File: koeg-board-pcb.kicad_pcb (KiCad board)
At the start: 2 copper layers, 112.5 x 84.2 mm, 108 parts, among them J1 Conn_01x02, J2 SWD_Connector, J3 USB_C_Receptacle_USB2.0_14P, Q1 BSS138, SW1 Reset Button, SW10 SW_Push, SW11 SW_Push, SW12 SW_Push, SW13 SW_Push, SW14 SW_Push, SW15 SW_Push, SW16 SW_Push, SW17 SW_Push, SW18 SW_Push, SW19 SW_Push, SW2 SW_On_Off, SW20 SW_Push, SW21 SW_Push, SW22 SW_Push, SW23 SW_Push, SW3 SW_Push, SW4 SW_Push, SW5 SW_Push, SW6 SW_Push, SW7 SW_Push, SW8 SW_Push, SW9 SW_Push, U1 nRF52840, U2 USBLC6-2SC6, U3 AMS1117-5.0, Y1 JYJE 2TJ432000NYFBC

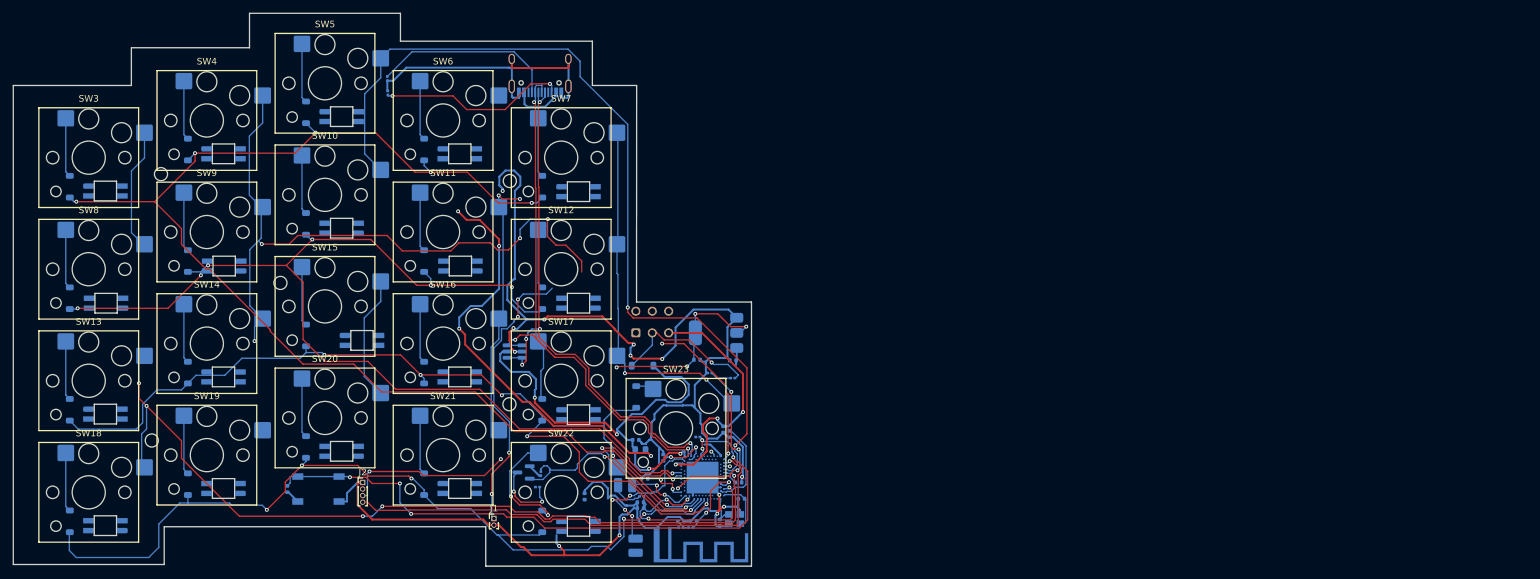
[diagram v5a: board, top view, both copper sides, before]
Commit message: routed left side
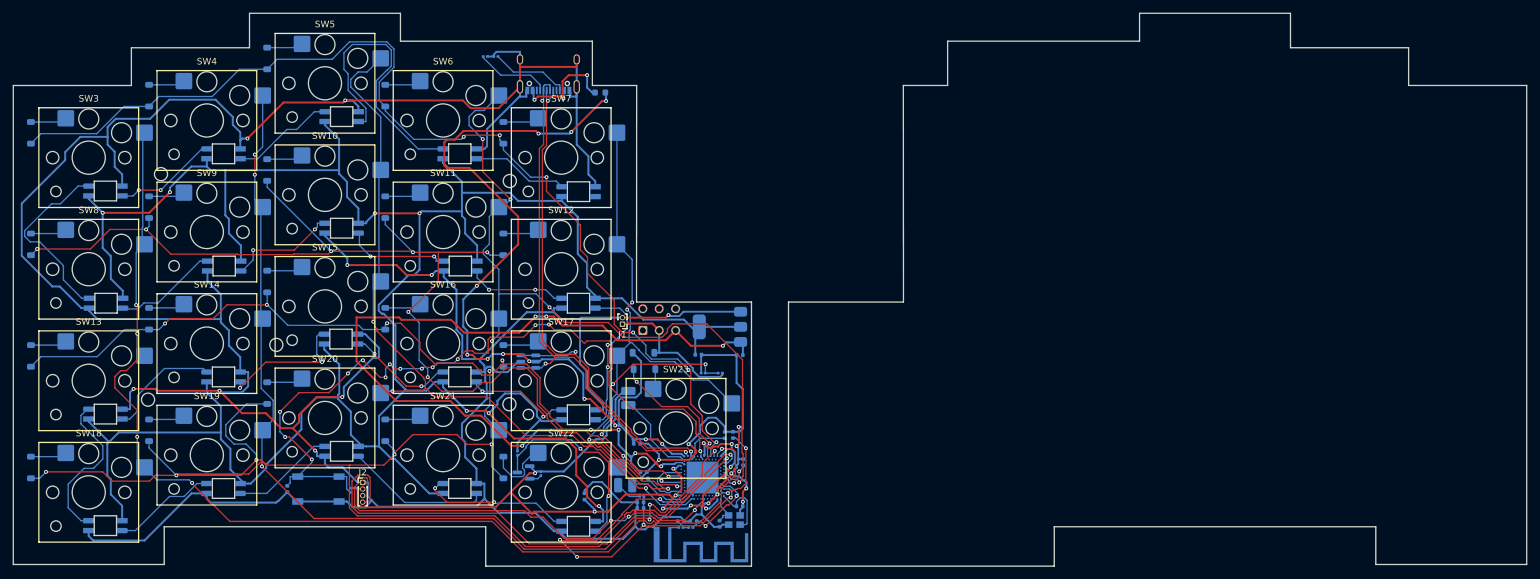
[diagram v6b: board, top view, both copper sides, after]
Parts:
- J3: footprint USB_Type_C:HRO-TYPE-C-31-M-12 -> Connector_USB:USB_C_Receptacle_XKB_U262-16XN-4BVC11
- moved F1 54.7 mm to (123.0, 55.8), turned to 180 degrees
- moved R1 53.5 mm to (85.1, 116.4), turned to -90 degrees
- moved J1 35.5 mm to (126.4, 91.1), turned to 180 degrees
- moved L3 22.5 mm to (127.3, 102.3), turned to 90 degrees
- moved R5 17.4 mm to (107.1, 50.3), turned to 180 degrees
- moved R4 15.3 mm to (105.5, 50.3), turned to 0 degrees
- moved C3 13.7 mm to (129.7, 113.6), turned to 0 degrees
- moved D2 10.1 mm to (36.3, 61.9)
- moved D12 10.1 mm to (36.3, 95.9)
- moved D13 10.1 mm to (54.3, 90.2)
- moved D17 10.1 mm to (36.3, 112.9)
- moved D18 10.1 mm to (54.3, 107.2)
- moved D3 10.1 mm to (54.3, 56.2)
- moved D7 10.1 mm to (36.3, 78.9)
- moved D8 10.1 mm to (54.3, 73.2)
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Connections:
- U1 pad A10: /left/ROW4 -> unconnected-(U1-AIN5/P0.29-PadA10)
- U1 pad A16: /left/ROW2 -> unconnected-(U1-P1.13-PadA16)
- U1 pad A8: /left/ROW0 -> /left/COL2
- U1 pad AD16: unconnected-(U1-P0.20-PadAD16) -> /left/ROW4
- U1 pad AD18: unconnected-(U1-P0.22-PadAD18) -> /left/ROW0
- U1 pad AD22: unconnected-(U1-TRACEDATA0/P1.00-PadAD22) -> /left/COL0
- U1 pad J1: unconnected-(U1-AIN2/P0.04-PadJ1) -> /left/ROW2
- U1 pad R24: /left/COL0 -> unconnected-(U1-P1.06-PadR24)
- U1 pad U24: /left/COL2 -> unconnected-(U1-P1.04-PadU24)
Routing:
- net LED_5V: track 29.8 -> 405.4 mm, vias 4 -> 7
- net GND: track 311.5 -> 652.2 mm, vias 13 -> 18
- net V_SYS: track 5.65 -> 127.8 mm, vias 0 -> 10
- net 3.2V-5V: track 42.2 -> 136.5 mm, vias 3 -> 8
- net /left/COL3: track 41.7 -> 127.5 mm, vias 3 -> 6
- net 5V: track 66.7 -> 129.9 mm, vias 4 -> 12
- net /left/ROW3: track 131.2 -> 188.4 mm, vias 5 -> 6
- net VBUS: track 73.0 -> 17.4 mm, vias 4 -> 3
- net VBAT: track 66.7 -> 22.0 mm, vias 5 -> 0
- net Net-(D39-DIN): track 0.00 -> 43.6 mm
- net /left/COL1: track 102.8 -> 144.1 mm, vias 5 -> 6
- net /left/COL2: track 151.0 -> 114.9 mm, vias 2 -> 3
- net /left/leds/LED_PIN: track 35.3 -> 1.89 mm, vias 2 -> 0
- net /left/ROW0: track 192.1 -> 160.3 mm
- net Net-(D37-DOUT): track 0.00 -> 28.5 mm
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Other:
- board size 112.5 x 84.2 mm -> 230.6 x 84.3 mm

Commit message: placed right side
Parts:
- added AE2: PCB_Antenna, pcb_ant:pcb_antenna, F.Cu at (167.2, 122.4)
- added C17: 4.7uF, Capacitor_SMD:C_0402_1005Metric, B.Cu at (156.7, 115.3)
- added C18: 100nF, Capacitor_SMD:C_0402_1005Metric, B.Cu at (227.4, 116.5)
- added C19: 4.7uF, Capacitor_SMD:C_0402_1005Metric, B.Cu at (156.7, 116.5)
- added C20: 100nF, Capacitor_SMD:C_0402_1005Metric, B.Cu at (174.6, 120.6)
- added C21: 100pF, Capacitor_SMD:C_0402_1005Metric, B.Cu at (172.5, 110.8)
- added C22: 820pF, Capacitor_SMD:C_0402_1005Metric, B.Cu at (156.7, 113.7)
- added C23: 1uF, Capacitor_SMD:C_0402_1005Metric, B.Cu at (174.8, 117.8)
- added C24: 47nF, Capacitor_SMD:C_0402_1005Metric, B.Cu at (174.8, 116.7)
- added C25: 4.7uF, Capacitor_SMD:C_0402_1005Metric, B.Cu at (156.7, 117.7)
- added C26: 4.7uF, Capacitor_SMD:C_0402_1005Metric, B.Cu at (174.6, 122.6)
- added C27: 12pF, Capacitor_SMD:C_0402_1005Metric, B.Cu at (177.3, 108.0)
- added C28: 12pF, Capacitor_SMD:C_0402_1005Metric, B.Cu at (172.7, 108.3)
- added C29: 1pF, Capacitor_SMD:C_0402_1005Metric, B.Cu at (171.2, 125.9)
- added C30: 1.2pF, Capacitor_SMD:C_0402_1005Metric, B.Cu at (171.2, 124.1)
- added C31: 1uF, Capacitor_SMD:C_0402_1005Metric, B.Cu at (156.7, 97.7)
- added C32: 1uF, Capacitor_SMD:C_0402_1005Metric, B.Cu at (156.8, 96.3)
- added D43: 1N5819, Diode_SMD:D_SOD-123, B.Cu at (173.0, 84.5)
- added D44: 1N5819, Diode_SMD:D_SOD-123, B.Cu at (247.0, 61.9)
- added D45: 1N5819, Diode_SMD:D_SOD-123, B.Cu at (229.0, 56.2)
- added D46: 1N5819, Diode_SMD:D_SOD-123, B.Cu at (211.0, 50.6)
- added D47: 1N5819, Diode_SMD:D_SOD-123, B.Cu at (193.0, 56.2)
- added D48: 1N5819, Diode_SMD:D_SOD-123, B.Cu at (175.0, 61.9)
- added D49: 1N5819, Diode_SMD:D_SOD-123, B.Cu at (247.0, 78.9)
- added D50: 1N5819, Diode_SMD:D_SOD-123, B.Cu at (229.0, 73.2)
- added D51: 1N5819, Diode_SMD:D_SOD-123, B.Cu at (211.0, 67.6)
- added D52: 1N5819, Diode_SMD:D_SOD-123, B.Cu at (193.0, 73.2)
- added D53: 1N5819, Diode_SMD:D_SOD-123, B.Cu at (175.0, 78.9)
- added D54: 1N5819, Diode_SMD:D_SOD-123, B.Cu at (247.0, 95.9)
- added D55: 1N5819, Diode_SMD:D_SOD-123, B.Cu at (229.0, 90.2)
- added D56: 1N5819, Diode_SMD:D_SOD-123, B.Cu at (211.0, 84.6)
- added D57: 1N5819, Diode_SMD:D_SOD-123, B.Cu at (193.0, 90.2)
- added D58: 1N5819, Diode_SMD:D_SOD-123, B.Cu at (175.0, 95.9)
- added D59: 1N5819, Diode_SMD:D_SOD-123, B.Cu at (247.0, 112.9)
- added D60: 1N5819, Diode_SMD:D_SOD-123, B.Cu at (229.0, 107.2)
- added D61: 1N5819, Diode_SMD:D_SOD-123, B.Cu at (211.0, 101.6)
- added D62: 1N5819, Diode_SMD:D_SOD-123, B.Cu at (193.0, 107.2)
- added D63: 1N5819, Diode_SMD:D_SOD-123, B.Cu at (175.0, 112.9)
- added D64: 1N5819, Diode_SMD:D_SOD-123, B.Cu at (159.1, 103.4)
- added D65: SK6812MINI, Keebio_Parts:SK6812-MINI-E, B.Cu at (185.2, 121.8)
- added D66: SK6812MINI, Keebio_Parts:SK6812-MINI-E, B.Cu at (203.2, 116.1)
- added D67: SK6812MINI, Keebio_Parts:SK6812-MINI-E, B.Cu at (221.3, 110.3)
- added D68: SK6812MINI, Keebio_Parts:SK6812-MINI-E, B.Cu at (239.2, 116.1)
- added D69: SK6812MINI, Keebio_Parts:SK6812-MINI-E, B.Cu at (257.2, 121.8)
- added D70: SK6812MINI, Keebio_Parts:SK6812-MINI-E, B.Cu at (185.2, 104.8)
- added D71: SK6812MINI, Keebio_Parts:SK6812-MINI-E, B.Cu at (203.2, 99.1)
- added D72: SK6812MINI, Keebio_Parts:SK6812-MINI-E, B.Cu at (221.2, 93.4)
- added D73: SK6812MINI, Keebio_Parts:SK6812-MINI-E, B.Cu at (239.2, 99.1)
- added D74: SK6812MINI, Keebio_Parts:SK6812-MINI-E, B.Cu at (257.3, 104.7)
- added D75: SK6812MINI, Keebio_Parts:SK6812-MINI-E, B.Cu at (185.2, 87.8)
- added D76: SK6812MINI, Keebio_Parts:SK6812-MINI-E, B.Cu at (203.2, 82.1)
- added D77: SK6812MINI, Keebio_Parts:SK6812-MINI-E, B.Cu at (221.2, 76.4)
- added D78: SK6812MINI, Keebio_Parts:SK6812-MINI-E, B.Cu at (239.3, 82.0)
- added D79: SK6812MINI, Keebio_Parts:SK6812-MINI-E, B.Cu at (257.3, 87.7)
- added D80: SK6812MINI, Keebio_Parts:SK6812-MINI-E, B.Cu at (185.2, 70.8)
- added D81: SK6812MINI, Keebio_Parts:SK6812-MINI-E, B.Cu at (203.2, 65.1)
- added D82: SK6812MINI, Keebio_Parts:SK6812-MINI-E, B.Cu at (221.2, 59.4)
- added D83: SK6812MINI, Keebio_Parts:SK6812-MINI-E, B.Cu at (239.2, 65.1)
- added D84: SK6812MINI, Keebio_Parts:SK6812-MINI-E, B.Cu at (257.2, 70.8)
- added F2: 500mA, Fuse:Fuse_0603_1608Metric, B.Cu at (186.7, 66.3)
- added H10: MountingHole, MountingHole:MountingHole_2mm, F.Cu at (192.3, 118.6)
- added H11: MountingHole, MountingHole:MountingHole_2mm, F.Cu at (160.7, 77.1)
- added H12: MountingHole, MountingHole:MountingHole_2mm, F.Cu at (135.6, 94.6)
- added H6: MountingHole, MountingHole:MountingHole_2mm, F.Cu at (179.4, 68.3)
- added H7: MountingHole, MountingHole:MountingHole_2mm, F.Cu at (247.3, 68.5)
- added H8: MountingHole, MountingHole:MountingHole_2mm, F.Cu at (247.4, 102.6)
- added H9: MountingHole, MountingHole:MountingHole_2mm, F.Cu at (439.2, 59.6)
- added J4: Conn_01x02, Connector_PinHeader_1.00mm:PinHeader_1x02_P1.00mm_Vertical, F.Cu at (174.0, 89.5)
- added J5: SWD_Connector, Connector_PinHeader_1.00mm:PinHeader_1x04_P1.00mm_Vertical, F.Cu at (214.4, 115.0)
- added J6: USB_C_Receptacle_USB2.0_14P, Connector_USB:USB_C_Receptacle_XKB_U262-16XN-4BVC11, B.Cu at (184.1, 51.7)
- added L10: 2.2nH, Inductor_SMD:L_0201_0603Metric, B.Cu at (171.0, 123.2)
- added L6: 10uH, Inductor_SMD:L_1008_2520Metric, B.Cu at (178.8, 119.5)
- added L7: 15nH, Inductor_SMD:L_0201_0603Metric, B.Cu at (174.5, 119.1)
- added L8: 10uH, Inductor_SMD:L_1008_2520Metric, B.Cu at (156.9, 120.3)
- added L9: 4.7nH, Inductor_SMD:L_0201_0603Metric, B.Cu at (171.0, 125.0)
- added Q2: BSS138, Package_TO_SOT_SMD:SOT-23, B.Cu at (178.1, 125.4)
- added R10: 10K, Resistor_SMD:R_0201_0603Metric, B.Cu at (177.6, 115.2)
- added R11: 5.1k, Resistor_SMD:R_0201_0603Metric, B.Cu at (190.5, 50.9)
- added R12: 5.1k, Resistor_SMD:R_0201_0603Metric, B.Cu at (190.5, 52.8)
- added R13: 10K, Resistor_SMD:R_0201_0603Metric, B.Cu at (175.7, 126.4)
- added R14: 10K, Resistor_SMD:R_0201_0603Metric, B.Cu at (180.6, 124.4)
- added R8: 100K, Resistor_SMD:R_0201_0603Metric, B.Cu at (216.4, 114.0)
- added R9: 10K, Resistor_SMD:R_0201_0603Metric, B.Cu at (174.9, 115.7)
- added SW24: Reset Button, Button_Switch_SMD:SW_SPST_TL3342, B.Cu at (221.6, 116.2)
- added SW25: SW_On_Off, Button_Switch_THT:SW_CK_JS202011AQN_DPDT_Angled, B.Cu at (165.5, 92.0)
- added SW26: SW_Push, PCM_Switch_Keyboard_Hotswap_Kailh:SW_Hotswap_Kailh_Choc_V1V2_1.00u, F.Cu at (255.1, 65.7)
- added SW27: SW_Push, PCM_Switch_Keyboard_Hotswap_Kailh:SW_Hotswap_Kailh_Choc_V1V2_1.00u, F.Cu at (237.1, 60.0)
- added SW28: SW_Push, PCM_Switch_Keyboard_Hotswap_Kailh:SW_Hotswap_Kailh_Choc_V1V2_1.00u, F.Cu at (219.1, 54.3)
- added SW29: SW_Push, PCM_Switch_Keyboard_Hotswap_Kailh:SW_Hotswap_Kailh_Choc_V1V2_1.00u, F.Cu at (201.1, 60.0)
- added SW30: SW_Push, PCM_Switch_Keyboard_Hotswap_Kailh:SW_Hotswap_Kailh_Choc_V1V2_1.00u, F.Cu at (183.1, 65.7)
- added SW31: SW_Push, PCM_Switch_Keyboard_Hotswap_Kailh:SW_Hotswap_Kailh_Choc_V1V2_1.00u, F.Cu at (255.1, 82.7)
- added SW32: SW_Push, PCM_Switch_Keyboard_Hotswap_Kailh:SW_Hotswap_Kailh_Choc_V1V2_1.00u, F.Cu at (237.1, 77.0)
- added SW33: SW_Push, PCM_Switch_Keyboard_Hotswap_Kailh:SW_Hotswap_Kailh_Choc_V1V2_1.00u, F.Cu at (219.1, 71.3)
- added SW34: SW_Push, PCM_Switch_Keyboard_Hotswap_Kailh:SW_Hotswap_Kailh_Choc_V1V2_1.00u, F.Cu at (201.1, 77.0)
- added SW35: SW_Push, PCM_Switch_Keyboard_Hotswap_Kailh:SW_Hotswap_Kailh_Choc_V1V2_1.00u, F.Cu at (183.1, 82.7)
- added SW36: SW_Push, PCM_Switch_Keyboard_Hotswap_Kailh:SW_Hotswap_Kailh_Choc_V1V2_1.00u, F.Cu at (255.1, 99.7)
- added SW37: SW_Push, PCM_Switch_Keyboard_Hotswap_Kailh:SW_Hotswap_Kailh_Choc_V1V2_1.00u, F.Cu at (237.1, 94.0)
- added SW38: SW_Push, PCM_Switch_Keyboard_Hotswap_Kailh:SW_Hotswap_Kailh_Choc_V1V2_1.00u, F.Cu at (219.1, 88.3)
- added SW39: SW_Push, PCM_Switch_Keyboard_Hotswap_Kailh:SW_Hotswap_Kailh_Choc_V1V2_1.00u, F.Cu at (201.1, 94.0)
- added SW40: SW_Push, PCM_Switch_Keyboard_Hotswap_Kailh:SW_Hotswap_Kailh_Choc_V1V2_1.00u, F.Cu at (183.1, 99.7)
- added SW41: SW_Push, PCM_Switch_Keyboard_Hotswap_Kailh:SW_Hotswap_Kailh_Choc_V1V2_1.00u, F.Cu at (255.1, 116.7)
- added SW42: SW_Push, PCM_Switch_Keyboard_Hotswap_Kailh:SW_Hotswap_Kailh_Choc_V1V2_1.00u, F.Cu at (237.1, 111.0)
- added SW43: SW_Push, PCM_Switch_Keyboard_Hotswap_Kailh:SW_Hotswap_Kailh_Choc_V1V2_1.00u, F.Cu at (219.1, 105.3)
- added SW44: SW_Push, PCM_Switch_Keyboard_Hotswap_Kailh:SW_Hotswap_Kailh_Choc_V1V2_1.00u, F.Cu at (201.1, 111.0)
- added SW45: SW_Push, PCM_Switch_Keyboard_Hotswap_Kailh:SW_Hotswap_Kailh_Choc_V1V2_1.00u, F.Cu at (183.1, 116.7)
- added SW46: SW_Push, PCM_Switch_Keyboard_Hotswap_Kailh:SW_Hotswap_Kailh_Choc_V1V2_1.75u_90deg, F.Cu at (165.6, 108.2)
- added U4: nRF52840, Package_DFN_QFN:Nordic_AQFN-73-1EP_7x7mm_P0.5mm, B.Cu at (167.2, 116.6)
- added U5: USBLC6-2SC6, Package_TO_SOT_SMD:SOT-23-6, B.Cu at (193.3, 67.3)
- added U6: AMS1117-5.0, Package_TO_SOT_SMD:SOT-223-3_TabPin2, B.Cu at (158.6, 91.5)
- added Y2: JYJE 2TJ432000NYFBC, Crystal:Crystal_SMD_2520-4Pin_2.5x2.0mm, B.Cu at (175.1, 108.1)
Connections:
- net 3.2V-5V renamed /left/3.2V-5V
- net 5V renamed /left/5V
- net LED_5V renamed /left/leds/LED_5V
- net VBAT renamed /left/VBAT
- net VBUS renamed /left/VBUS
- net V_SYS renamed /left/V_SYS
- Q1 pad 2: /left/leds/LED_PIN -> /left/LED_PIN
- R6 pad 2: /left/leds/LED_PIN -> /left/LED_PIN
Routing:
- net GND: track 652.2 -> 656.7 mm, vias 18 -> 20
- net /left/leds/LED_PIN: track 1.89 -> 0.00 mm
- net /left/LED_PIN: track 0.00 -> 1.89 mm
- net /right/3.2V-5V: track 0.00 -> 1.14 mm
- net Net-(AE2-PCB_Trace): track 0.00 -> 0.61 mm, vias 0 -> 1
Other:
- board size 230.6 x 84.3 mm -> 232.9 x 84.2 mm

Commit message: routed right side, added filets
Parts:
- AE2: moved to B.Cu
- J3, J6: footprint Connector_USB:USB_C_Receptacle_XKB_U262-16XN-4BVC11 -> Connector_USB:USB_C_Receptacle_G-Switch_GT-USB-7025
- moved H9 348.6 mm to (93.1, 101.6)
- moved L10 135.2 mm to (36.1, 132.3)
- moved L9 135.0 mm to (36.2, 131.4)
- moved C30 133.6 mm to (37.8, 132.3)
- moved C29 133.5 mm to (37.8, 131.4)
- moved AE2 133.4 mm to (34.2, 132.9), turned to 0 degrees
- moved D61 123.2 mm to (88.2, 112.1)
- moved D67 123.2 mm to (98.6, 120.9)
- moved SW43 123.2 mm to (96.3, 115.9)
- moved D56 123.2 mm to (88.2, 95.1)
- moved D72 123.2 mm to (98.5, 104.0)
- moved SW38 123.2 mm to (96.3, 98.9)
- moved D51 123.2 mm to (88.2, 78.1)
- moved D77 123.2 mm to (98.5, 87.0)
- moved SW33 123.2 mm to (96.3, 81.9)
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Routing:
- net GND: track 656.7 -> 1250.2 mm, vias 20 -> 34
- net /right/leds/LED_5V: track 0.00 -> 423.9 mm, vias 0 -> 9
- net /right/COL1: track 0.00 -> 215.8 mm, vias 0 -> 14
- net /right/COL0: track 0.00 -> 215.1 mm, vias 0 -> 8
- net /right/ROW1: track 0.00 -> 181.6 mm, vias 0 -> 8
- net /right/ROW0: track 0.00 -> 162.0 mm, vias 0 -> 6
- net /right/ROW2: track 0.00 -> 137.4 mm, vias 0 -> 8
- net /right/COL4: track 0.00 -> 127.2 mm, vias 0 -> 7
- net /right/COL2: track 0.00 -> 122.8 mm, vias 0 -> 5
- net /right/COL3: track 0.00 -> 120.9 mm, vias 0 -> 7
- net /right/SWDIO: track 0.00 -> 114.3 mm, vias 0 -> 3
- net /right/V_SYS: track 0.00 -> 113.9 mm, vias 0 -> 8
- net /right/D-: track 0.00 -> 104.2 mm, vias 0 -> 3
- net /right/D+: track 0.00 -> 98.9 mm, vias 0 -> 3
- net /right/ROW3: track 0.00 -> 94.0 mm, vias 0 -> 3
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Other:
- board size 232.9 x 84.2 mm -> 229.8 x 84.3 mm
